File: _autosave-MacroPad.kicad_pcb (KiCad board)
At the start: 2 copper layers, 111.6 x 82.3 mm, 42 parts, among them J1 Conn_01x04_Pin, SW1 SW_Push, SW10 SW_Push, SW11 SW_Push, SW12 SW_Push, SW13 RotaryEncoder_Switch, SW14 RotaryEncoder_Switch, SW2 SW_Push, SW3 SW_Push, SW4 SW_Push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

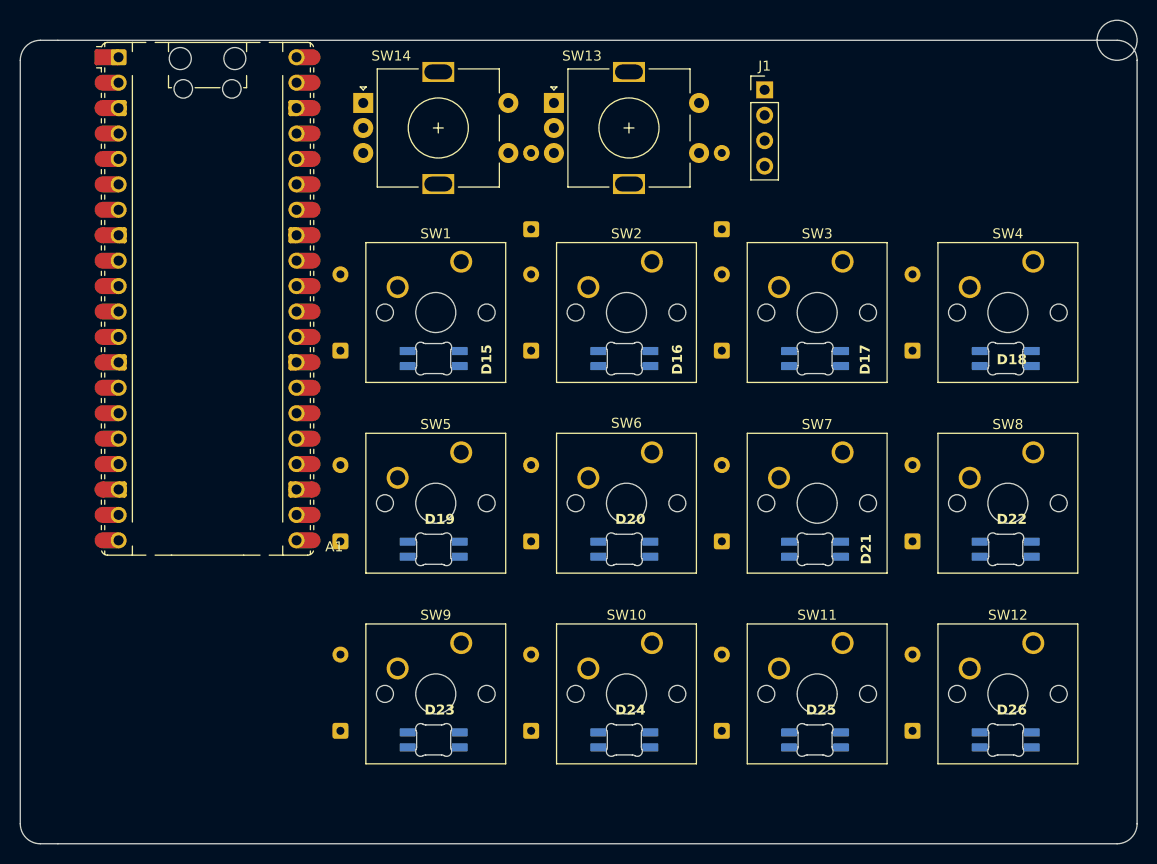
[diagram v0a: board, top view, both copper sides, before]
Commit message: feat: switched switches
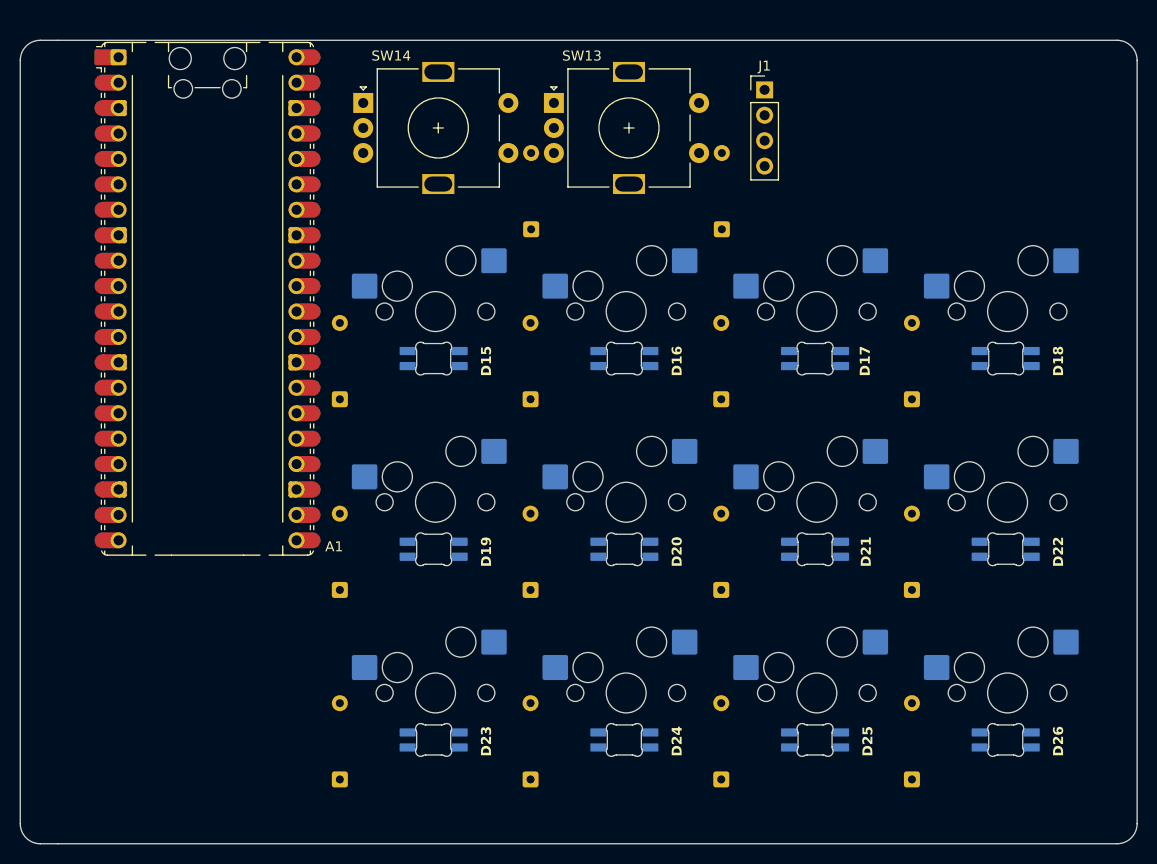
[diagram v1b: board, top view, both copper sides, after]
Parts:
- SW1, SW10, SW11, SW12, SW2, SW3, SW4, SW5, SW6, SW7, SW8, SW9: footprint Button_Switch_Keyboard:SW_Cherry_MX_1.00u_PCB -> Switch_MX_Hotswap:MX-Hotswap-1U; moved to B.Cu
- moved SW1 5.61 mm to (136.5, 80.9), turned to 180 degrees
- moved SW5 5.61 mm to (136.5, 100.0), turned to 180 degrees
- moved SW9 5.61 mm to (136.5, 119.0), turned to 180 degrees
- moved SW10 5.61 mm to (155.5, 119.0), turned to 180 degrees
- moved SW11 5.61 mm to (174.6, 119.0), turned to 180 degrees
- moved SW12 5.61 mm to (193.6, 119.0), turned to 180 degrees
- moved SW2 5.61 mm to (155.5, 80.9), turned to 180 degrees
- moved SW3 5.61 mm to (174.6, 80.9), turned to 180 degrees
- moved SW4 5.61 mm to (193.6, 80.9), turned to 180 degrees
- moved SW6 5.61 mm to (155.5, 100.0), turned to 180 degrees
- moved SW7 5.61 mm to (174.6, 100.0), turned to 180 degrees
- moved SW8 5.61 mm to (193.6, 100.0), turned to 180 degrees
- moved D1 4.86 mm to (126.9, 89.7)
- moved D10 4.86 mm to (146.0, 127.7)
- moved D11 4.86 mm to (165.0, 127.7)
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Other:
- board size 111.6 x 82.3 mm -> 111.6 x 80.3 mm
